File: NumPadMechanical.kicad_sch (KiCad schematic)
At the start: 54 parts, among them J1 USB_C_Receptacle_USB2.0_14P, U1 STM32F103CBTx, U2 AMS1117-3.3

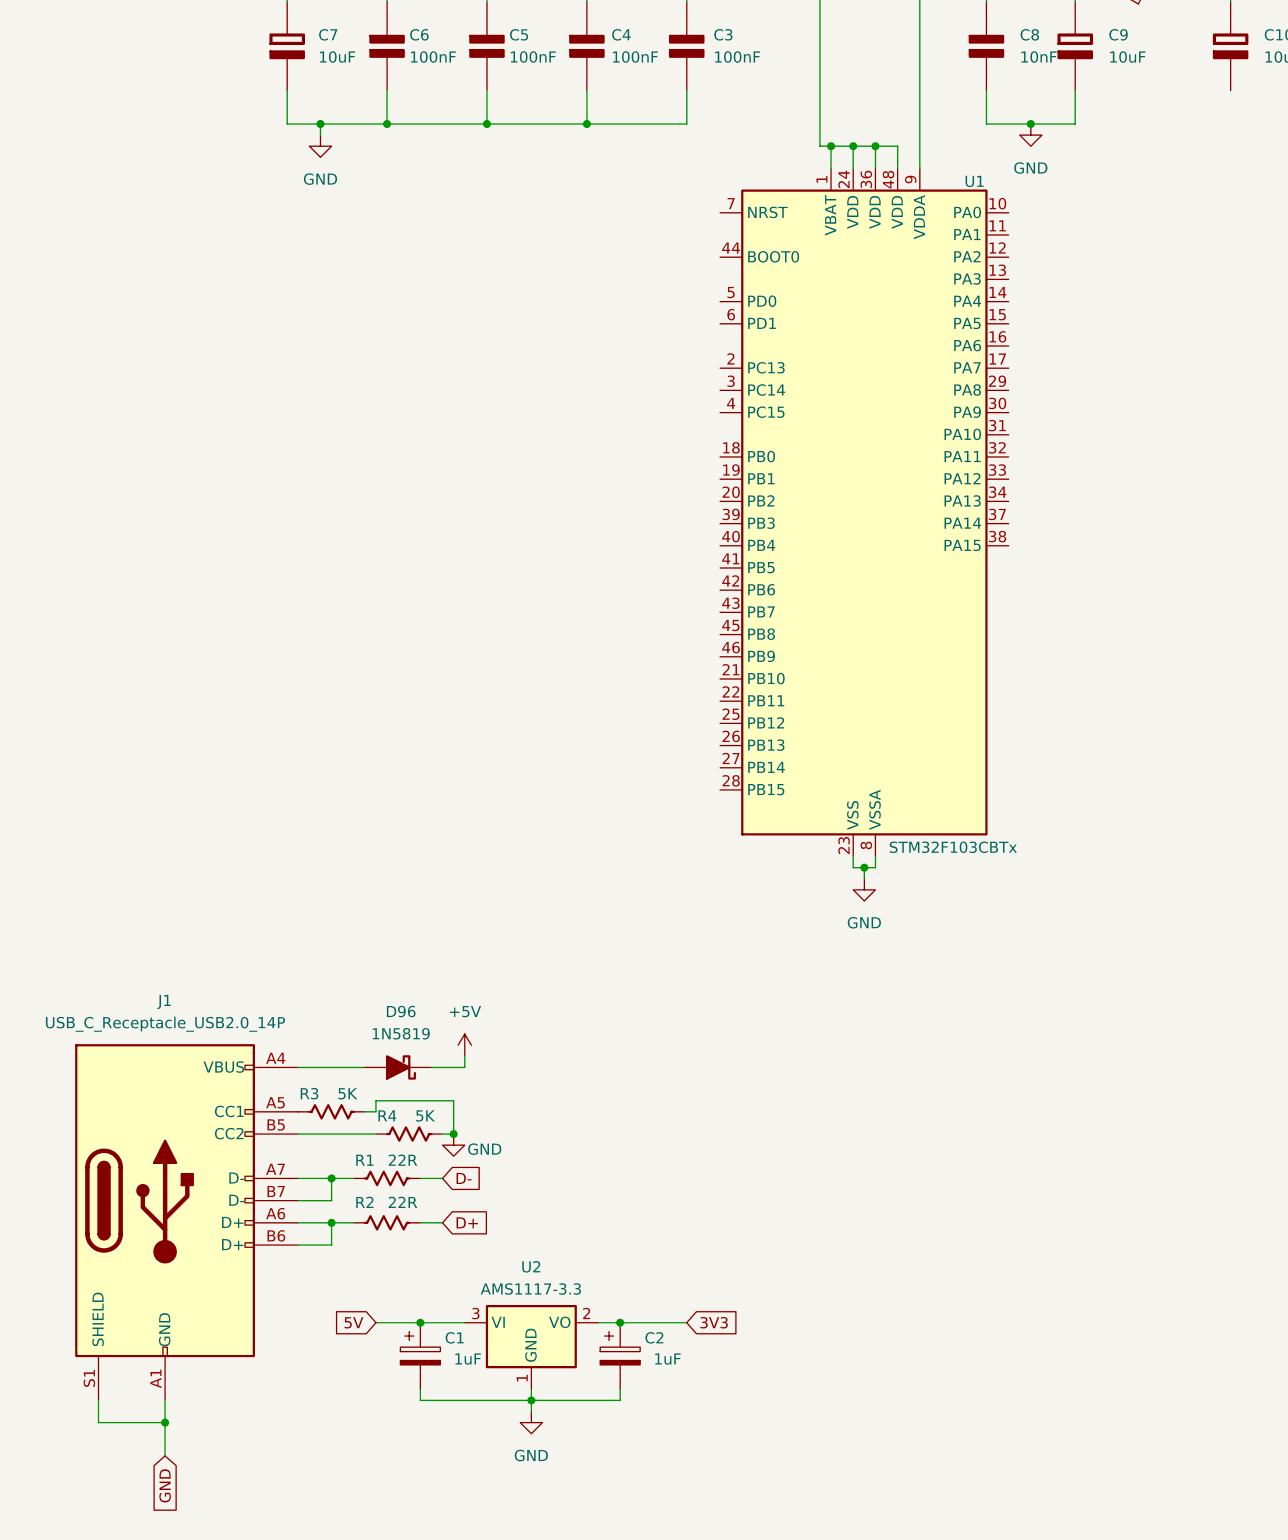
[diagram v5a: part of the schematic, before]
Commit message: Agregado cristal oscilador y corregido el conector usb, se agregan footprints de algunos dispositivos
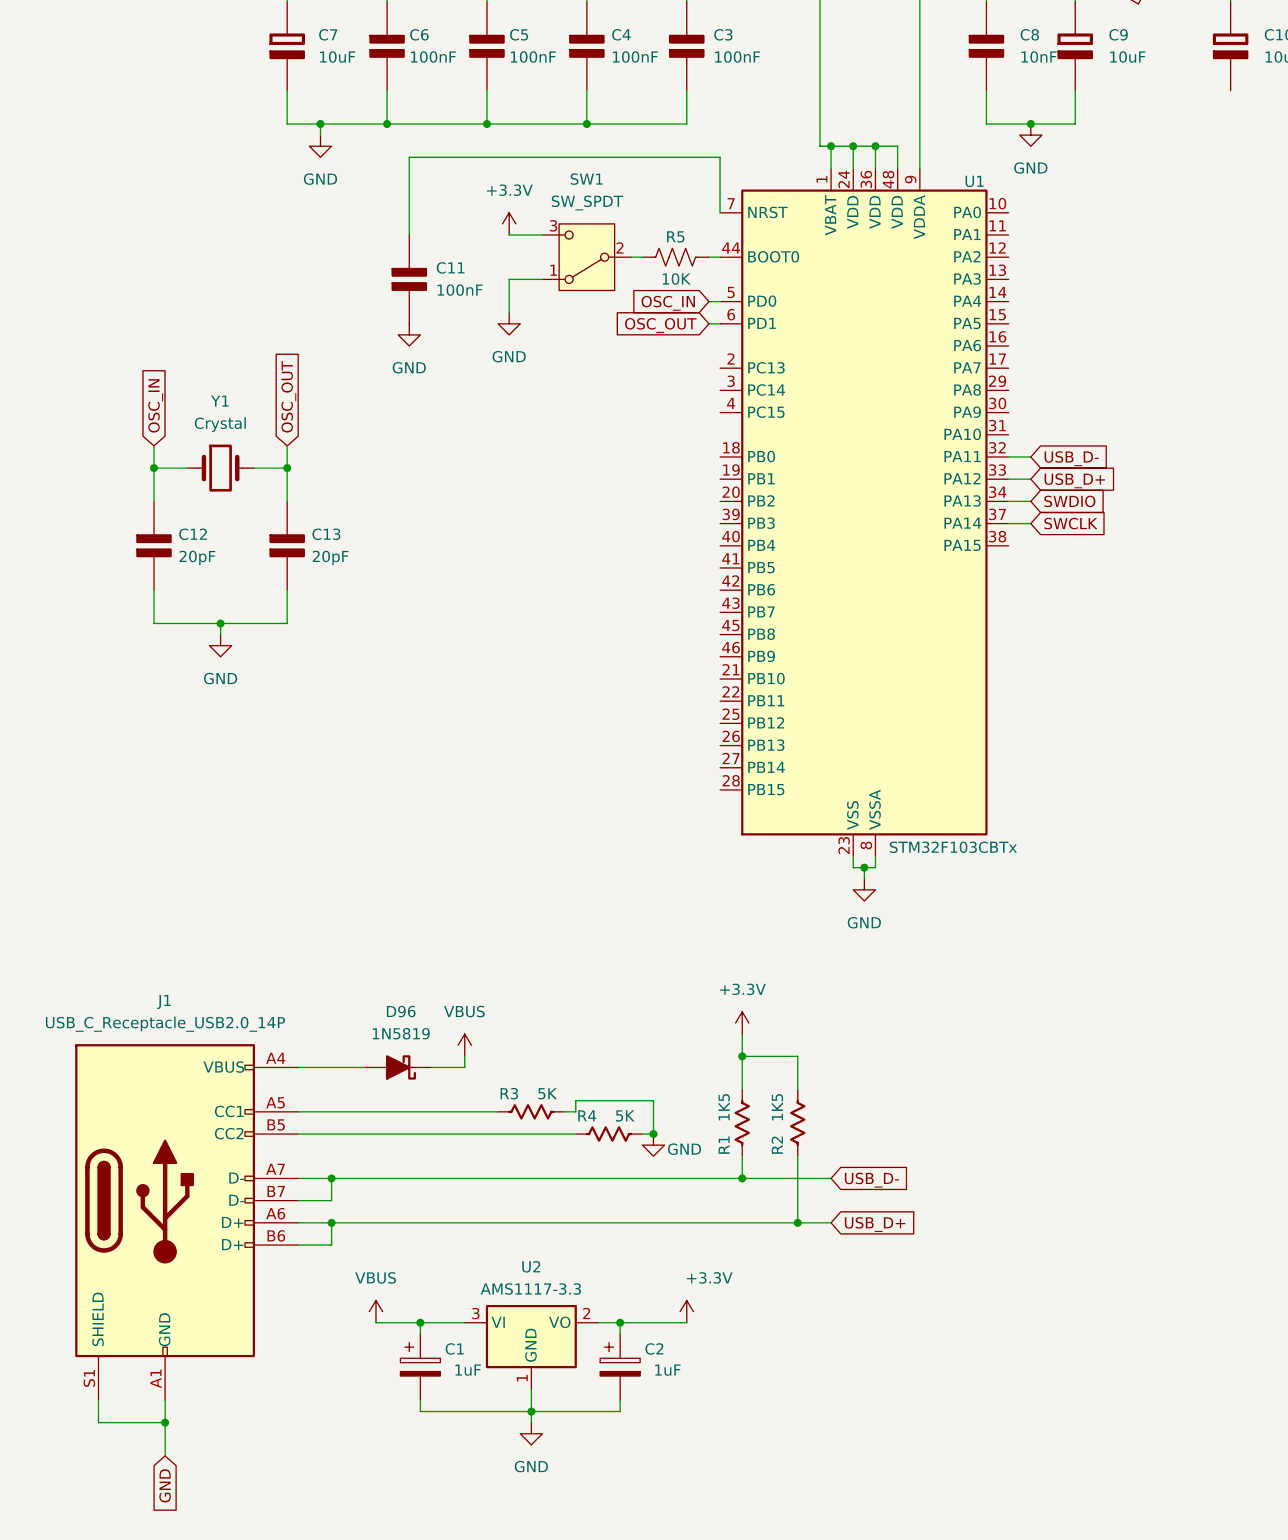
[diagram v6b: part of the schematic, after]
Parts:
- added C11: 100nF, Capacitor_SMD:C_0603_1608Metric_Pad1.08x0.95mm_HandSolder, symbol PCM_Elektuur:C
- added C12, C13: 20pF, Capacitor_SMD:C_0603_1608Metric_Pad1.08x0.95mm_HandSolder, symbol PCM_Elektuur:C
- added R5: 10K, Resistor_SMD:R_0603_1608Metric_Pad0.98x0.95mm_HandSolder, symbol Device:R_US
- added SW1: SW_SPDT, symbol Switch:SW_SPDT
- added Y1: Crystal, Crystal:Crystal_SMD_HC49-SD_HandSoldering, symbol Device:Crystal
- C3, C4, C5, C6: footprint (none) -> Capacitor_SMD:C_0603_1608Metric_Pad1.08x0.95mm_HandSolder
- R1, R2: value 22R -> 1K5
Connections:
- net 3V3 is gone; now on net +3.3V: C2.1, U2.2 (VO)
- net 5V is gone; now on net VBUS: C1.1, U2.3 (VI)
- net D+ is gone; now on net +3.3V: R2.2
- net D- is gone; now on net +3.3V: R1.2
- net +3.3V: now also SW1.3 (C)
- net GND: now also C11.2 (-), C12.2 (-), C13.2 (-), SW1.1 (A)
- net USB_D+: now reaches J1.A6 (D+), J1.B6 (D+), R2.1
- net USB_D+: now also U1.33 (PA12)
- net USB_D-: now reaches J1.A7 (D-), J1.B7 (D-), R1.1
- net USB_D-: now also U1.32 (PA11)
- net SWDIO: now reaches U1.34 (PA13)
- net SWCLK: now reaches U1.37 (PA14)
- net at U1.44 (BOOT0): now also R5.1
- net OSC_IN: now reaches U1.5 (PD0)
- net OSC_IN: now also C12.1 (+), Y1.1
- net OSC_OUT: now reaches U1.6 (PD1)
- net OSC_OUT: now also C13.1 (+), Y1.2
- net at U1.7 (NRST): now also C11.1 (+)
- net +5V renamed VBUS
- new net: R5.2, SW1.2 (B)
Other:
- moved on the sheet: C1, C2, R1, R3, R4

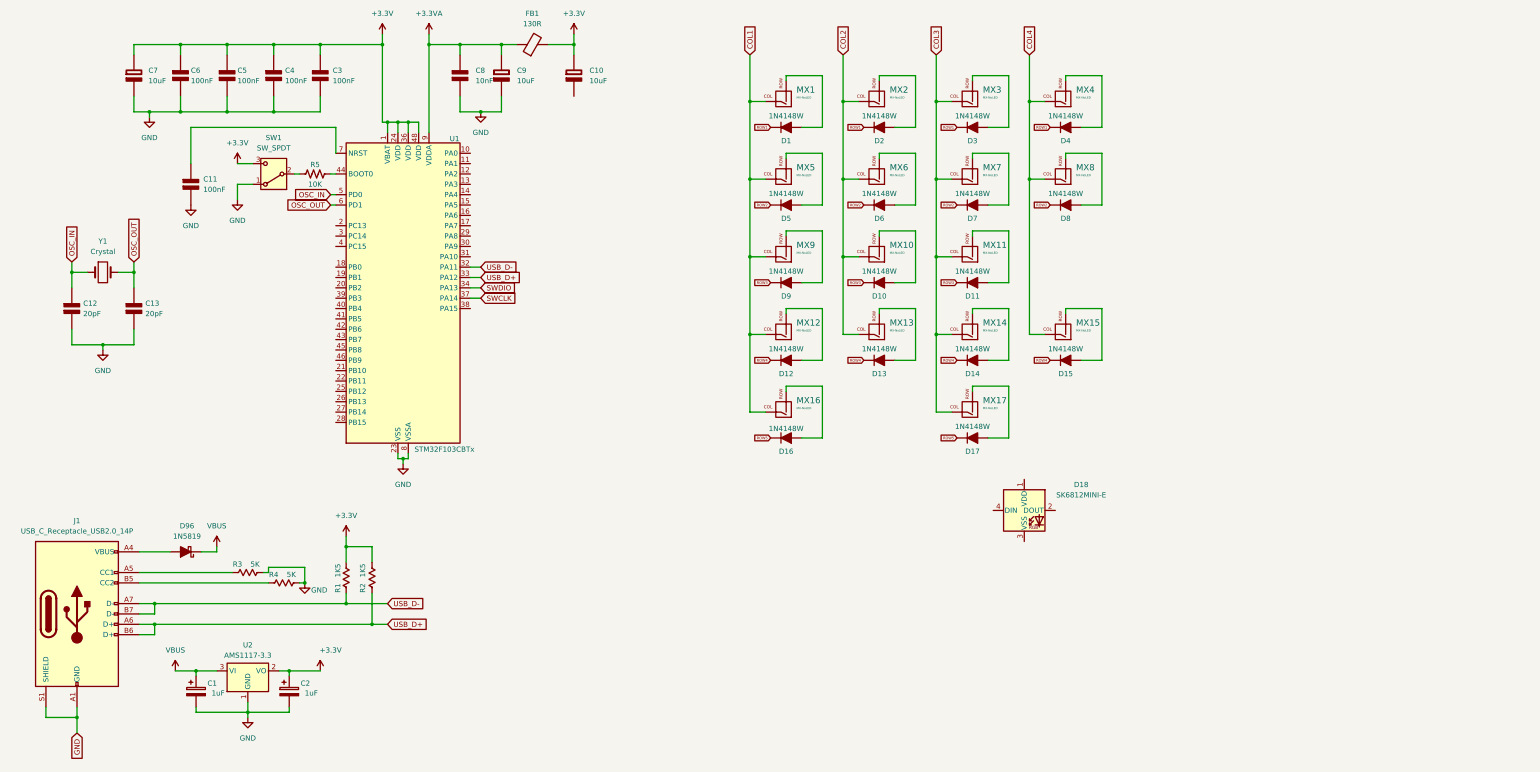
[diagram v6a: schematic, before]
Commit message: Modificado el esquematico finalizando conexiones, se añaden leds rgb y de señalizacion, se agregan footprints de todos los elementos faltantes y se realiza acomodo de pcb preliminar
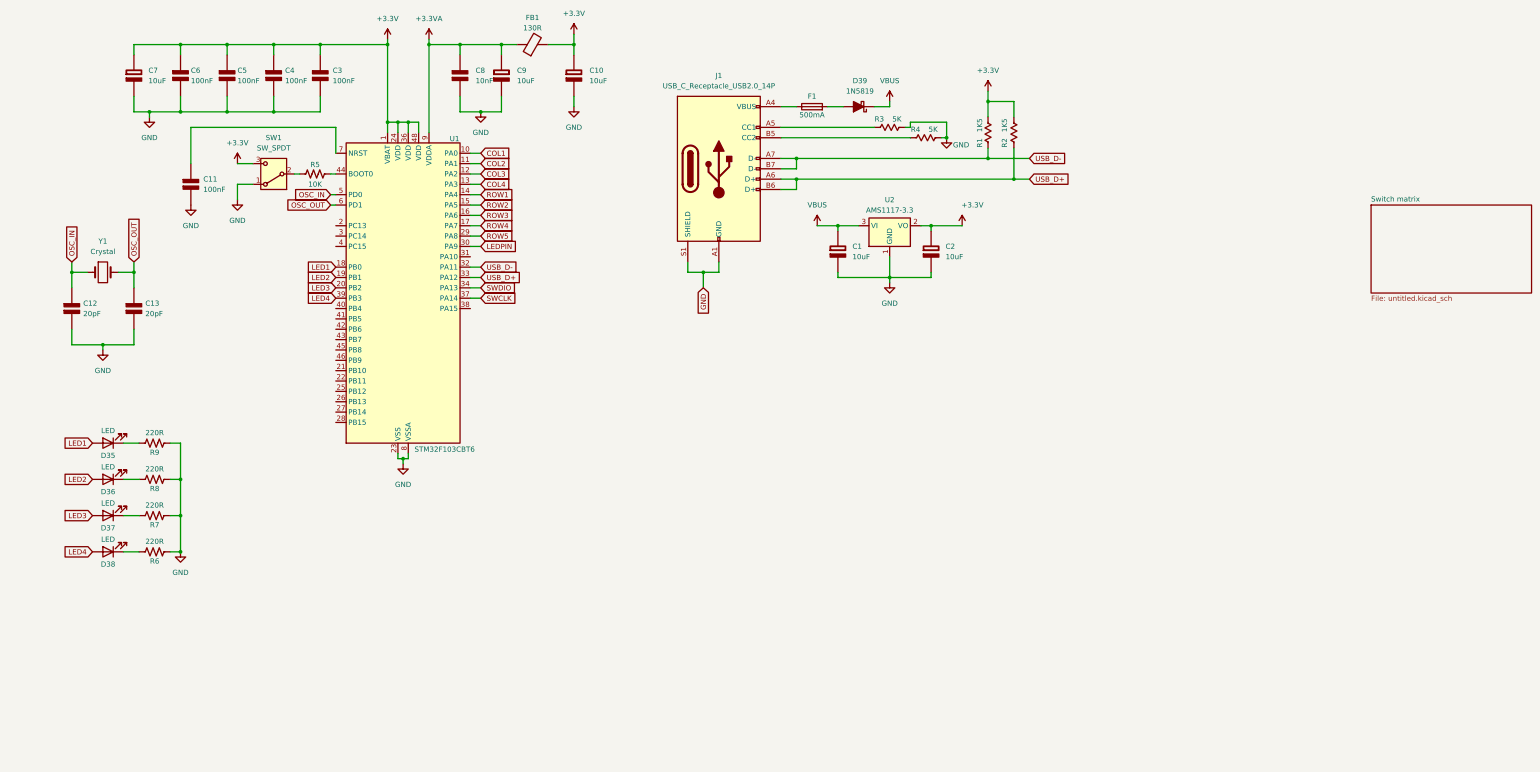
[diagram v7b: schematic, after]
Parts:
- removed C1, C2: 1uF, Capacitor_SMD:CP_Elec_6.3x7.7, symbol PCM_Capacitor_AKL:CP_SMD_D6.3mm_H7.7mm
- removed D1, D10, D11, D12, D13, D14, D15, D16, D17, D2, D3, D4, D5, D6, D7, D8, D9: 1N4148W, D_SOD-123_A:D_SOD-123_A, symbol PCM_Diode_AKL:1N4148W
- removed D18: SK6812MINI-E, kicad-keyboard-parts:MX_SK6812MINI-E, symbol kicad-keyboard-parts:SK6812MINI-E
- removed MX1, MX10, MX11, MX12, MX13, MX14, MX17, MX2, MX3, MX4, MX5, MX6, MX7, MX9: MX-NoLED, MX_Alps_Hybrid:MX-1U-NoLED, symbol MX_Alps_Hybrid:MX-NoLED
- removed MX15, MX8: MX-NoLED, MX_Alps_Hybrid:MX-Alps-Hybrid-2U-Vertical, symbol MX_Alps_Hybrid:MX-NoLED
- removed MX16: MX-NoLED, MX_Alps_Hybrid:MX-2U-NoLED, symbol MX_Alps_Hybrid:MX-NoLED
- added C1, C2: 10uF, Capacitor_SMD:C_0603_1608Metric, symbol PCM_Elektuur:C-polar
- added D35, D36, D37, D38: LED, LED_SMD:LED_0603_1608Metric, symbol Device:LED
- added F1: 500mA, Fuse:Fuse_0603_1608Metric, symbol Device:Fuse
- added R6, R7, R8, R9: 220R, Resistor_SMD:R_0603_1608Metric, symbol Device:R_US
- C10, C7, C8, C9: footprint (none) -> Capacitor_SMD:C_0603_1608Metric
- FB1: footprint (none) -> Inductor_SMD:L_0603_1608Metric
- R1, R2, R3, R4, R5: footprint Resistor_SMD:R_0603_1608Metric_Pad0.98x0.95mm_HandSolder -> Resistor_SMD:R_0603_1608Metric
- SW1: footprint (none) -> Button_Switch_THT:SW_Slide_SPDT_Straight_CK_OS102011MS2Q
- U1: value STM32F103CBTx -> STM32F103CBT6
- Y1: footprint Crystal:Crystal_SMD_HC49-SD_HandSoldering -> Crystal:Crystal_SMD_HC49-SD
- renumbered D96 to D39
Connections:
- net +3.3V: now also C2.1 (+)
- net COL1: now also U1.10 (PA0)
- net COL2: now also U1.11 (PA1)
- net COL3: now also U1.12 (PA2)
- net COL4: now also U1.13 (PA3)
- net GND: now also C10.2 (-), C1.2 (-), C2.2 (-), R6.2, R7.2, R8.2, R9.2
- net ROW1: now also U1.14 (PA4)
- net ROW2: now also U1.15 (PA5)
- net ROW3: now also U1.16 (PA6)
- net ROW4: now also U1.17 (PA7)
- net ROW5: now also U1.29 (PA8)
- net VBUS: now also C1.1 (+)
- net at J1.A4 (VBUS), J1.A9 (VBUS), J1.B4 (VBUS)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: now also F1.1; no longer D39.2 (A)
- net LED1: now reaches U1.18 (PB0)
- net LED1: now also D35.2 (A)
- net LED2: now reaches U1.19 (PB1)
- net LED2: now also D36.2 (A)
- net LED3: now reaches U1.20 (PB2)
- net LED3: now also D37.2 (A)
- net LEDPIN: now reaches U1.30 (PA9)
- net LED4: now reaches U1.39 (PB3)
- net LED4: now also D38.2 (A)
- new net: D38.1 (K), R6.1
- new net: D39.2 (A), F1.2
- new net: D37.1 (K), R7.1
- new net: D35.1 (K), R9.1
- new net: D36.1 (K), R8.1
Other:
- added sheet Switch matrix (untitled.kicad_sch)
- moved on the sheet: D39, J1, R1, R2, R3, R4, U2

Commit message: Se hacen modificaciones en la pcb acomodando los dispositivos y se agrega tierra comun en ambos lados de la placa
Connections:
- no-connect marks 0 -> 17
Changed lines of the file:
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@@
 	)
 	(junction
+		(at 121.92 20.32)
+		(diameter 0)
+		(color 0 0 0 0)
+	)
+	(junction
 		(at 45.72 36.83)
 		(diameter 0)
@@
 	)
 	(junction
-		(at 121.92 20.32)
-		(diameter 0)
-		(color 0 0 0 0)
-	)
-	(junction
 		(at 237.49 64.77)
 		(diameter 0)
@@
 	)
 	(junction
-		(at 114.3 20.32)
-		(diameter 0)
-		(color 0 0 0 0)
-	)
-	(junction
 		(at 132.08 20.32)
 		(diameter 0)
@@
 	)
 	(junction
+		(at 114.3 20.32)
+		(diameter 0)
+		(color 0 0 0 0)
+	)
+	(junction
 		(at 76.2 36.83)
 		(diameter 0)
 		(color 0 0 0 0)
 	)
+	(no_connect
+		(at 91.44 67.31)
+	)
+	(no_connect
+		(at 124.46 72.39)
+	)
+	(no_connect
+		(at 91.44 92.71)
+	)
+	(no_connect
+		(at 91.44 95.25)
+	)
+	(no_connect
+		(at 91.44 85.09)
+	)
+	(no_connect
+		(at 91.44 113.03)
+	)
+	(no_connect
+		(at 91.44 90.17)
+	)
+	(no_connect
+		(at 91.44 64.77)
+	)
+	(no_connect
+		(at 124.46 85.09)
+	)
+	(no_connect
+		(at 91.44 69.85)
+	)
+	(no_connect
+		(at 91.44 100.33)
+	)
+	(no_connect
+		(at 91.44 87.63)
+	)
+	(no_connect
+		(at 91.44 105.41)
+	)
+	(no_connect
+		(at 91.44 97.79)
+	)
+	(no_connect
+		(at 91.44 107.95)
+	)
+	(no_connect
+		(at 91.44 102.87)
+	)
+	(no_connect
+		(at 91.44 110.49)
+	)
 	(wire
 		(pts
@@
 	(wire
 		(pts
-			(xy 114.3 19.05) (xy 114.3 20.32)
-		)
-		(stroke
-			(width 0)
-			(type default)
-		)
-	)
-	(wire
-		(pts
-			(xy 114.3 20.32) (xy 121.92 20.32)
-		)
-		(stroke
-			(width 0)
-			(type default)
-		)
-	)
-	(wire
-		(pts
 			(xy 87.63 20.32) (xy 87.63 22.86)
 		)
@@
 	(wire
 		(pts
+			(xy 114.3 20.32) (xy 121.92 20.32)
+		)
+		(stroke
+			(width 0)
+			(type default)
+		)
+	)
+	(wire
+		(pts
 			(xy 124.46 46.99) (xy 127 46.99)
 		)
@@
 	(wire
 		(pts
-			(xy 114.3 20.32) (xy 114.3 41.91)
+			(xy 114.3 19.05) (xy 114.3 20.32)
 		)
 		(stroke
@@
 	(wire
 		(pts
+			(xy 121.92 20.32) (xy 132.08 20.32)
+		)
+		(stroke
+			(width 0)
+			(type default)
+		)
+	)
+	(wire
+		(pts
+			(xy 114.3 20.32) (xy 114.3 41.91)
+		)
+		(stroke
+			(width 0)
+			(type default)
+		)
+	)
+	(wire
+		(pts
 			(xy 143.51 20.32) (xy 149.86 20.32)
 		)
@@
 	(wire
 		(pts
-			(xy 132.08 20.32) (xy 121.92 20.32)
-		)
-		(stroke
-			(width 0)
-			(type default)
-		)
-	)
-	(wire
-		(pts
 			(xy 124.46 52.07) (xy 127 52.07)
 		)
@@
 	)
 	(symbol
+		(lib_id "power:+3.3VA")
+		(at 114.3 19.05 0)
+		(unit 1)
+		(exclude_from_sim no)
+		(in_bom yes)
+		(on_board yes)
+		(dnp no)
+		(fields_autoplaced yes)
+		(property "Reference" "#PWR08"
+			(at 114.3 22.86 0)
+			(effects
+				(font
+					(size 1.27 1.27)
+				)
+				(hide yes)
+			)
+		)
+		(property "Value" "+3.3VA"
+			(at 114.3 13.97 0)
+			(effects
+				(font
+					(size 1.27 1.27)
+				)
+			)
+		)
+		(property "Footprint" ""
+			(at 114.3 19.05 0)
+			(effects
+				(font
+					(size 1.27 1.27)
+				)
+				(hide yes)
+			)
+		)
+		(property "Datasheet" ""
+			(at 114.3 19.05 0)
+			(effects
+				(font
+					(size 1.27 1.27)
+				)
+				(hide yes)
+			)
+		)
+		(property "Description" "Power symbol creates a global label with name \"+3.3VA\""
+			(at 114.3 19.05 0)
+			(effects
+				(font
+					(size 1.27 1.27)
+				)
+				(hide yes)
+			)
+		)
+		(pin "1"
+		)
+		(instances
+			(project "NumPadMechanical"
+				(path "/ac8bb69a-1f0c-4a45-9dd5-31d7563e18f7"
+					(reference "#PWR08")
+					(unit 1)
+				)
+			)
+		)
+	)
+	(symbol
 		(lib_id "PCM_Elektuur:C")
 		(at 55.88 54.61 0)
@@
 					(unit 1)
 				)
-			)
-		)
-	)
-	(symbol
-		(lib_id "power:+3.3VA")
-		(at 114.3 19.05 0)
-		(unit 1)
-		(exclude_from_sim no)
-		(in_bom yes)
-		(on_board yes)
-		(dnp no)
-		(fields_autoplaced yes)
-		(property "Reference" "#PWR08"
-			(at 114.3 22.86 0)
-			(effects
-				(font
-					(size 1.27 1.27)
-				)
-				(hide yes)
-			)
-		)
-		(property "Value" "+3.3VA"
-			(at 114.3 13.97 0)
-			(effects
-				(font
-					(size 1.27 1.27)
-				)
-			)
-		)
-		(property "Footprint" ""
-			(at 114.3 19.05 0)
-			(effects
-				(font
-					(size 1.27 1.27)
-				)
-				(hide yes)
-			)
-		)
-		(property "Datasheet" ""
-			(at 114.3 19.05 0)
-			(effects
-				(font
-					(size 1.27 1.27)
-				)
-				(hide yes)
-			)
-		)
-		(property "Description" "Power symbol creates a global label with name \"+3.3VA\""
-			(at 114.3 19.05 0)
-			(effects
-				(font
-					(size 1.27 1.27)
-				)
-				(hide yes)
-			)
-		)
-		(pin "1"
-		)
-		(instances
-			(project "NumPadMechanical"
-				(path "/ac8bb69a-1f0c-4a45-9dd5-31d7563e18f7"
-					(reference "#PWR08")
-					(unit 1)
-				)
